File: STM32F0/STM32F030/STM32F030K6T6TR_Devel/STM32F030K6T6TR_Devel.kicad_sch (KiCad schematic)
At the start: 18 parts, among them J1 Conn_01x06, J2 Conn_02x03_Odd_Even, J4 Conn_01x16, J5 Conn_01x16, J7 Conn_02x03_Odd_Even, U2 AMS1117-3.3

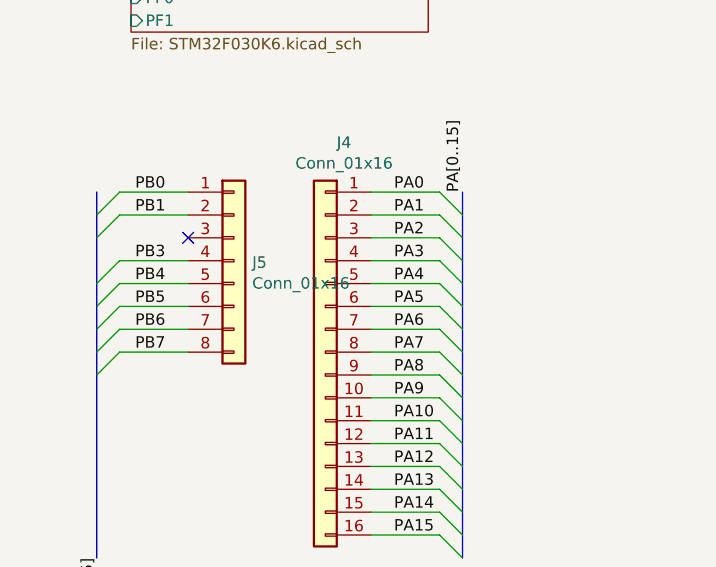
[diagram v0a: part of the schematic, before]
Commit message: Add mpn for pcbway
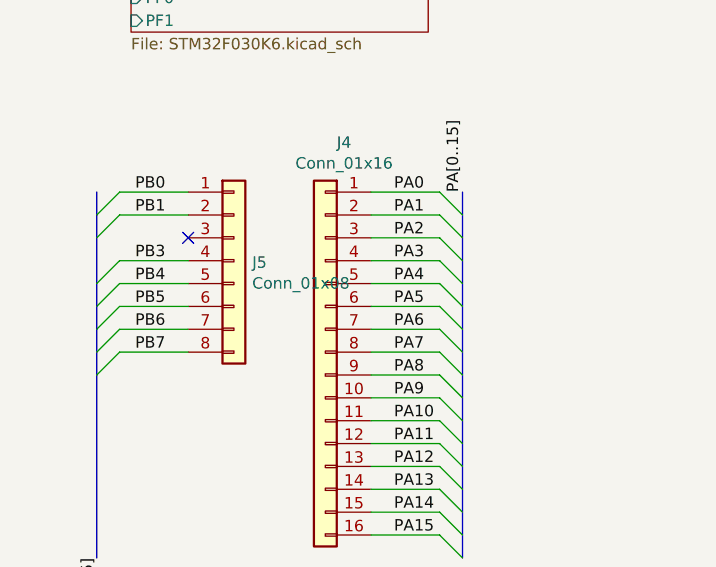
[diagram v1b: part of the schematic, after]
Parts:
- C10, C14: Manufacturer (none) -> KEMET; mpn (none) -> T491A106K010AT
- D1: Manufacturer (none) -> Würth Elektronik; mpn (none) -> 150080RS75000
- D2: Manufacturer (none) -> Würth Elektronik; mpn (none) -> 150080BS75000
- D3: Manufacturer (none) -> Würth Elektronik; mpn (none) -> 150080GS75000
- J5: value Conn_01x16 -> Conn_01x08
- R2: Manufacturer (none) -> Bourns Inc.; mpn (none) -> CR0805-FX-1002ELF
- R4, R6: Manufacturer (none) -> Bourns Inc.; mpn (none) -> CR0805-FX-1001ELF
- U2: Manufacturer (none) -> EVVO; mpn (none) -> AMS1117-3.3

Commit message: Revision LCSC
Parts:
- C10, C14: mpn T491A106K010AT -> T491A106K010AT
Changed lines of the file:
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@@
 			)
 		)
-		(property "mpn" " T491A106K010AT"
+		(property "mpn" "T491A106K010AT"
 			(at 248.92 127 0)
 			(effects
@@
 			)
 		)
-		(property "mpn" " T491A106K010AT"
+		(property "mpn" "T491A106K010AT"
 			(at 213.36 127 0)
 			(effects
